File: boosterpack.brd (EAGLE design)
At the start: 75.2 x 55.9 mm, 38 parts, among them J1 POWERPOLE_DOUBLE, J2 PHOENIXSCREWTERMINAL_2, J3 PHOENIXSCREWTERMINAL_2

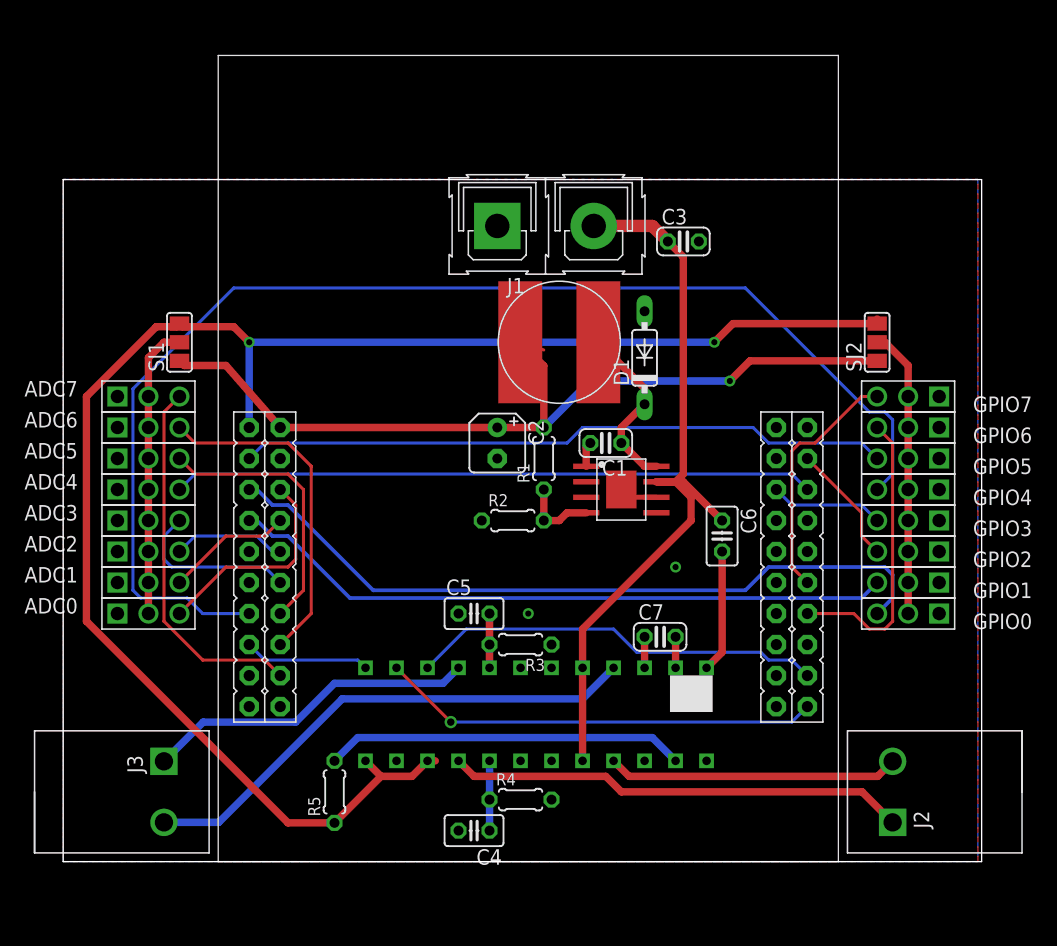
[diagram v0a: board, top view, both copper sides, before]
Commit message: added mounting holes; moved motors to a better spot
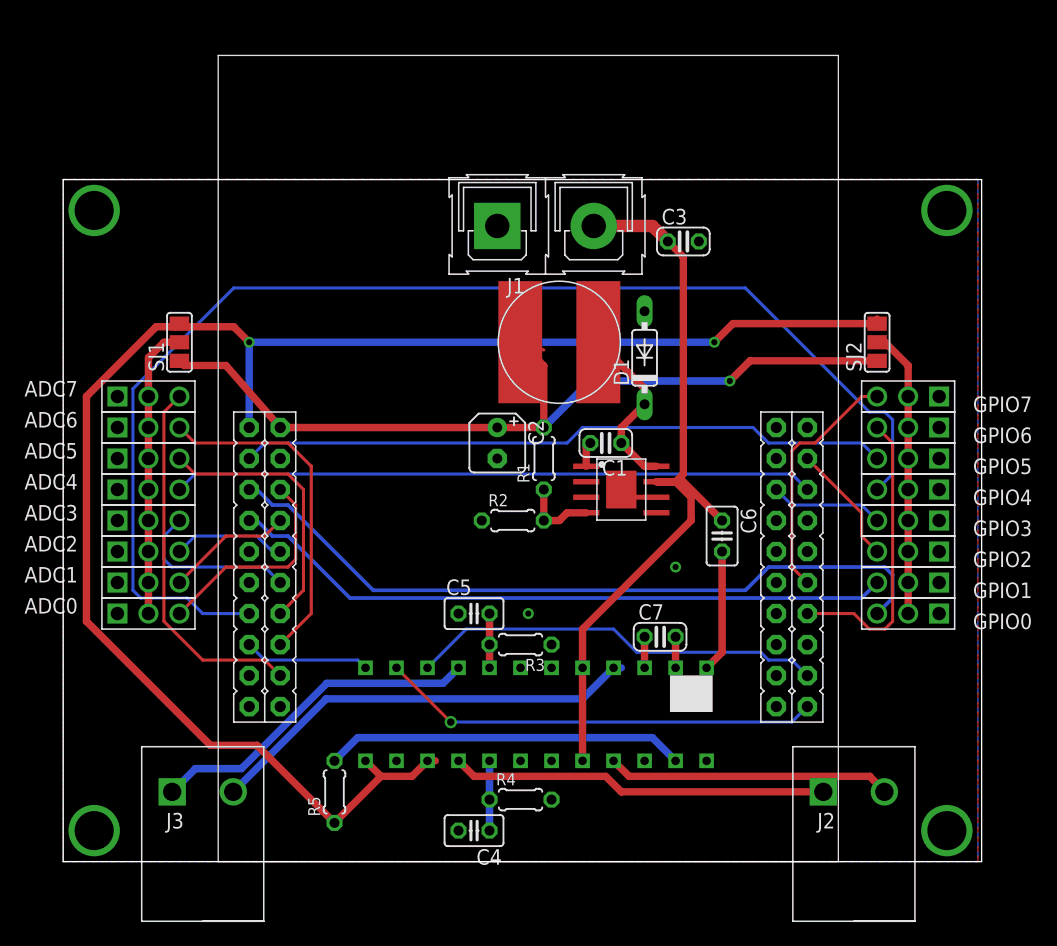
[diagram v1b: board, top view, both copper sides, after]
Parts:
- moved J3 3.18 mm to (21.6, 31.1), turned to 0 degrees
- moved J2 3.17 mm to (74.9, 31.1), turned to 0 degrees
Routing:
- net N$17: track 37.6 -> 30.9 mm
- net N$14: track 42.1 -> 36.0 mm
- net N$18: track 23.9 -> 23.3 mm
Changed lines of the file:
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@@
 <setting verticaltext="up"/>
 </settings>
-<grid distance="0.025" unitdist="inch" unit="inch" style="lines" multiple="1" display="yes" altdistance="0.025" altunitdist="inch" altunit="inch"/>
+<grid distance="0.025" unitdist="inch" unit="inch" style="dots" multiple="1" display="yes" altdistance="0.025" altunitdist="inch" altunit="inch"/>
 <layers>
 <layer number="1" name="Top" color="4" fill="1" visible="yes" active="yes"/>
@@
 <text x="83.82" y="47.625" size="1.27" layer="23">6</text>
 <text x="83.82" y="45.085" size="1.27" layer="23">7</text>
-<text x="85.09" y="38.735" size="1.27" layer="23" rot="R90">Port B</text>
-<text x="16.51" y="43.18" size="1.27" layer="23" rot="R270">Power</text>
-<text x="19.05" y="43.18" size="1.27" layer="23" rot="R270">Signal</text>
-<text x="13.97" y="43.18" size="1.27" layer="23" rot="R270">Ground</text>
-<text x="11.43" y="43.18" size="1.27" layer="23" rot="R270">Port E</text>
+<text x="85.09" y="39.37" size="1.27" layer="23" rot="R90">Port B</text>
+<text x="16.51" y="43.815" size="1.27" layer="23" rot="R270">Power</text>
+<text x="19.05" y="43.815" size="1.27" layer="23" rot="R270">Signal</text>
+<text x="13.97" y="43.815" size="1.27" layer="23" rot="R270">Ground</text>
+<text x="11.43" y="43.815" size="1.27" layer="23" rot="R270">Port E</text>
 <text x="12.7" y="65.405" size="1.27" layer="23" rot="R90">Port D</text>
 <text x="11.43" y="62.865" size="1.27" layer="23">0</text>
@@
 <text x="80.645" y="66.675" size="1.27" layer="23" rot="R180">5V</text>
 <text x="81.915" y="70.485" size="1.27" layer="23" rot="R180">3V3</text>
-<text x="76.2" y="43.18" size="1.27" layer="23" rot="R270">Signal</text>
-<text x="78.74" y="43.18" size="1.27" layer="23" rot="R270">Power</text>
-<text x="81.28" y="43.18" size="1.27" layer="23" rot="R270">Ground</text>
+<text x="76.2" y="43.815" size="1.27" layer="23" rot="R270">Signal</text>
+<text x="78.74" y="43.815" size="1.27" layer="23" rot="R270">Power</text>
+<text x="81.28" y="43.815" size="1.27" layer="23" rot="R270">Ground</text>
 </plain>
 <attributes>
@@
 <element name="D1" library="diode" package="DO35-7" value="" x="57.785" y="66.675" rot="R90"/>
 <element name="U$3" library="RASEagleLib" package="DIP24" value="A3992A" x="62.865" y="33.655" rot="R90"/>
-<element name="J2" library="RASEagleLib" package="PHOENIXSCREWTERMINAL_2" value="PHOENIXSCREWTERMINAL_2" x="78.105" y="31.115" rot="R90"/>
-<element name="J3" library="RASEagleLib" package="PHOENIXSCREWTERMINAL_2" value="PHOENIXSCREWTERMINAL_2" x="18.415" y="31.115" rot="R270"/>
+<element name="J2" library="RASEagleLib" package="PHOENIXSCREWTERMINAL_2" value="PHOENIXSCREWTERMINAL_2" x="74.93" y="31.115"/>
+<element name="J3" library="RASEagleLib" package="PHOENIXSCREWTERMINAL_2" value="PHOENIXSCREWTERMINAL_2" x="21.59" y="31.115"/>
 <element name="R3" library="resistor" package="0204/5" value="" x="47.625" y="43.18" rot="R180"/>
 <element name="R4" library="resistor" package="0204/5" value="" x="47.625" y="30.48"/>
@@
 <contactref element="J2" pad="1"/>
 <contactref element="U$3" pad="16"/>
-<wire x1="78.105" y1="28.615" x2="75.605" y2="31.115" width="0.6096" layer="1"/>
-<wire x1="75.605" y1="31.115" x2="55.88" y2="31.115" width="0.6096" layer="1"/>
+<wire x1="72.43" y1="31.115" x2="55.88" y2="31.115" width="0.6096" layer="1"/>
 <wire x1="55.88" y1="31.115" x2="54.61" y2="32.385" width="0.6096" layer="1"/>
 <wire x1="54.61" y1="32.385" x2="43.815" y2="32.385" width="0.6096" layer="1"/>
@@
 <contactref element="J2" pad="2"/>
 <contactref element="U$3" pad="21"/>
-<wire x1="78.105" y1="33.615" x2="76.875" y2="32.385" width="0.6096" layer="1"/>
-<wire x1="76.875" y1="32.385" x2="56.515" y2="32.385" width="0.6096" layer="1"/>
+<wire x1="77.43" y1="31.115" x2="76.24" y2="32.385" width="0.6096" layer="1"/>
+<wire x1="76.24" y1="32.385" x2="56.515" y2="32.385" width="0.6096" layer="1"/>
 <wire x1="56.515" y1="32.385" x2="55.245" y2="33.655" width="0.6096" layer="1"/>
 </signal>
@@
 <wire x1="63.5" y1="67.945" x2="25.4" y2="67.945" width="0.6096" layer="16"/>
 <wire x1="25.4" y1="60.96" x2="25.4" y2="67.945" width="0.6096" layer="16"/>
-<wire x1="32.385" y1="28.575" x2="28.575" y2="28.575" width="0.6096" layer="1"/>
-<wire x1="28.575" y1="28.575" x2="12.065" y2="45.085" width="0.6096" layer="1"/>
 <wire x1="12.065" y1="45.085" x2="12.065" y2="63.5" width="0.6096" layer="1"/>
 <wire x1="12.065" y1="63.5" x2="17.78" y2="69.215" width="0.6096" layer="1"/>
@@
 <wire x1="38.735" y1="32.385" x2="40.005" y2="33.655" width="0.6096" layer="1"/>
 <wire x1="40.005" y1="33.655" x2="40.64" y2="33.655" width="0.6096" layer="1"/>
+<wire x1="12.065" y1="45.085" x2="22.225" y2="34.925" width="0.6096" layer="1"/>
+<wire x1="22.225" y1="34.925" x2="26.035" y2="34.925" width="0.6096" layer="1"/>
+<wire x1="26.035" y1="34.925" x2="32.385" y2="28.575" width="0.6096" layer="1"/>
 </signal>
 <signal name="N$14">
 <contactref element="U$3" pad="4"/>
 <contactref element="J3" pad="2"/>
-<wire x1="18.415" y1="28.615" x2="22.9" y2="28.615" width="0.6096" layer="16"/>
-<wire x1="22.9" y1="28.615" x2="33.02" y2="38.735" width="0.6096" layer="16"/>
-<wire x1="33.02" y1="38.735" x2="52.705" y2="38.735" width="0.6096" layer="16"/>
+<wire x1="24.09" y1="31.115" x2="31.71" y2="38.735" width="0.6096" layer="16"/>
+<wire x1="31.71" y1="38.735" x2="52.705" y2="38.735" width="0.6096" layer="16"/>
 <wire x1="52.705" y1="38.735" x2="55.245" y2="41.275" width="0.6096" layer="16"/>
+<wire x1="55.245" y1="41.275" x2="55.88" y2="41.275" width="0.6096" layer="16"/>
 </signal>
 <signal name="N$15">
 <contactref element="J3" pad="1"/>
 <contactref element="U$3" pad="9"/>
-<wire x1="18.415" y1="33.615" x2="21.63" y2="36.83" width="0.6096" layer="16"/>
-<wire x1="21.63" y1="36.83" x2="29.21" y2="36.83" width="0.6096" layer="16"/>
-<wire x1="29.21" y1="36.83" x2="32.385" y2="40.005" width="0.6096" layer="16"/>
-<wire x1="32.385" y1="40.005" x2="41.275" y2="40.005" width="0.6096" layer="16"/>
+<wire x1="19.09" y1="31.115" x2="20.995" y2="33.02" width="0.6096" layer="16"/>
+<wire x1="20.995" y1="33.02" x2="24.765" y2="33.02" width="0.6096" layer="16"/>
+<wire x1="24.765" y1="33.02" x2="31.75" y2="40.005" width="0.6096" layer="16"/>
+<wire x1="31.75" y1="40.005" x2="41.275" y2="40.005" width="0.6096" layer="16"/>
 <wire x1="41.275" y1="40.005" x2="42.545" y2="41.275" width="0.6096" layer="16"/>
 </signal>
+<signal name="N$16">
+<via x="12.7" y="78.74" extent="1-16" drill="3.2"/>
+</signal>
+<signal name="N$24">
+<via x="82.55" y="78.74" extent="1-16" drill="3.2"/>
+</signal>
+<signal name="N$25">
+</signal>
+<signal name="N$26">
+<via x="82.55" y="27.94" extent="1-16" drill="3.2"/>
+</signal>
+<signal name="N$27">
+<via x="12.7" y="27.94" extent="1-16" drill="3.2"/>
+</signal>
 </signals>

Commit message: Removed motor drivers, almost done wiring board
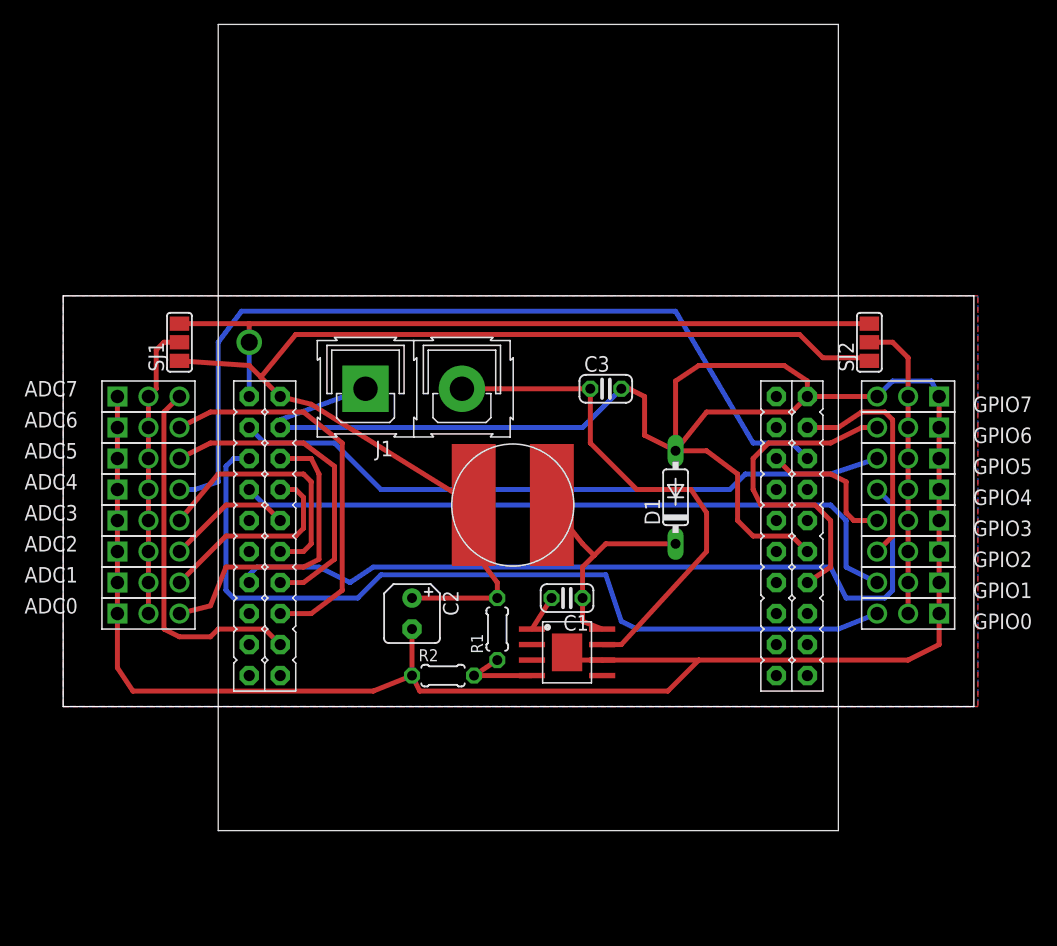
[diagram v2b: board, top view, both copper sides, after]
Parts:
- removed C4, C5: 0.1uF, resistor:C025-025X050
- removed C6: (no value), resistor:C025-025X050
- removed C7: 0.22uF, resistor:C025-024X044
- removed J2, J3: PHOENIXSCREWTERMINAL_2, RASEagleLib:PHOENIXSCREWTERMINAL_2
- removed R3, R4: (no value), resistor:0204/5
- removed R5: 5k, resistor:0204/5
- removed U$3: A3992A, RASEagleLib:DIP24
- moved J1 17.2 mm to (34.9, 64.1)
- moved C2 15.6 mm to (38.7, 45.7)
- moved R1 14.5 mm to (45.7, 44.5)
- moved U$2 14.1 mm to (51.4, 42.5)
- moved R2 13.9 mm to (41.3, 40.6)
- moved L1 13.9 mm to (47.0, 54.6)
- moved C3 13.6 mm to (54.6, 64.1)
- moved C1 13.1 mm to (51.4, 47.0)
- moved D1 11.7 mm to (60.3, 55.2)
- moved U$1 2.54 mm to (22.9, 94.0)
- moved SJ2 0.63 mm to (76.2, 67.9)
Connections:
- removed net CP2: C7.1, U$3.3
- removed net N$14: J3.2, U$3.4
- removed net N$15: J3.1, U$3.9
- removed net N$17: J2.1, U$3.16
- removed net N$18: J2.2, U$3.21
- removed net N$19: C5.2, R3.2, U$3.8
- removed net N$20: C4.1, R4.1, U$3.17
- removed net N$21: C6.2, U$3.1
- removed net N$22: R5.2, U$3.23
- removed net N$23: C7.2, U$3.2
- net +3V3: no longer R5.1, U$3.13, U$3.15
- net GND: no longer C4.2, C5.1, R3.1, R4.2, U$3.18, U$3.19, U$3.6, U$3.7
- net MOTORCLK: no longer U$3.11
- net MOTORFSS: no longer U$3.10
- net MOTORMOSI: no longer U$3.12
- net VCC: no longer C6.1, U$3.20, U$3.5
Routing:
- net GND: track 3.51 -> 198.8 mm, vias 2 -> 0
- net +3V3: track 133.6 -> 62.5 mm, vias 2 -> 1
- net N$2: track 103.2 -> 64.9 mm
- net MOTORCLK: track 36.0 -> 0.00 mm, vias 1 -> 0
- net N$14: track 36.0 -> 0.00 mm
- net MOTORFSS: track 34.0 -> 0.00 mm
- net N$17: track 30.9 -> 0.00 mm
- net N$22: track 29.5 -> 0.00 mm
- net N$15: track 27.7 -> 0.00 mm
- net N$18: track 23.3 -> 0.00 mm
- net +5V: track 72.3 -> 95.2 mm, vias 1 -> 0
- net VCC: track 62.4 -> 42.2 mm
- net N$13: track 52.5 -> 70.9 mm
- net N$8: track 20.1 -> 34.9 mm
- net MOTORMOSI: track 10.3 -> 0.00 mm
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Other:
- board size 75.2 x 55.9 mm -> 74.6 x 33.6 mm
